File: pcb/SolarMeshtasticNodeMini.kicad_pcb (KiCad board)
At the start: 4 copper layers, 33 x 47 mm, 30 parts, among them J2 Conn_01x02_Socket, J3 Conn_01x04_Socket, J4 Conn_01x02_Pin, J5 Conn_01x04_Socket, SW1 SSSS811101, SW2 SW_Push, U1 BQ25185, U2 HT-CT62, U3 HE9073A30MR, U4 APX803L05-32SA-7, U9 SS26_C5350986

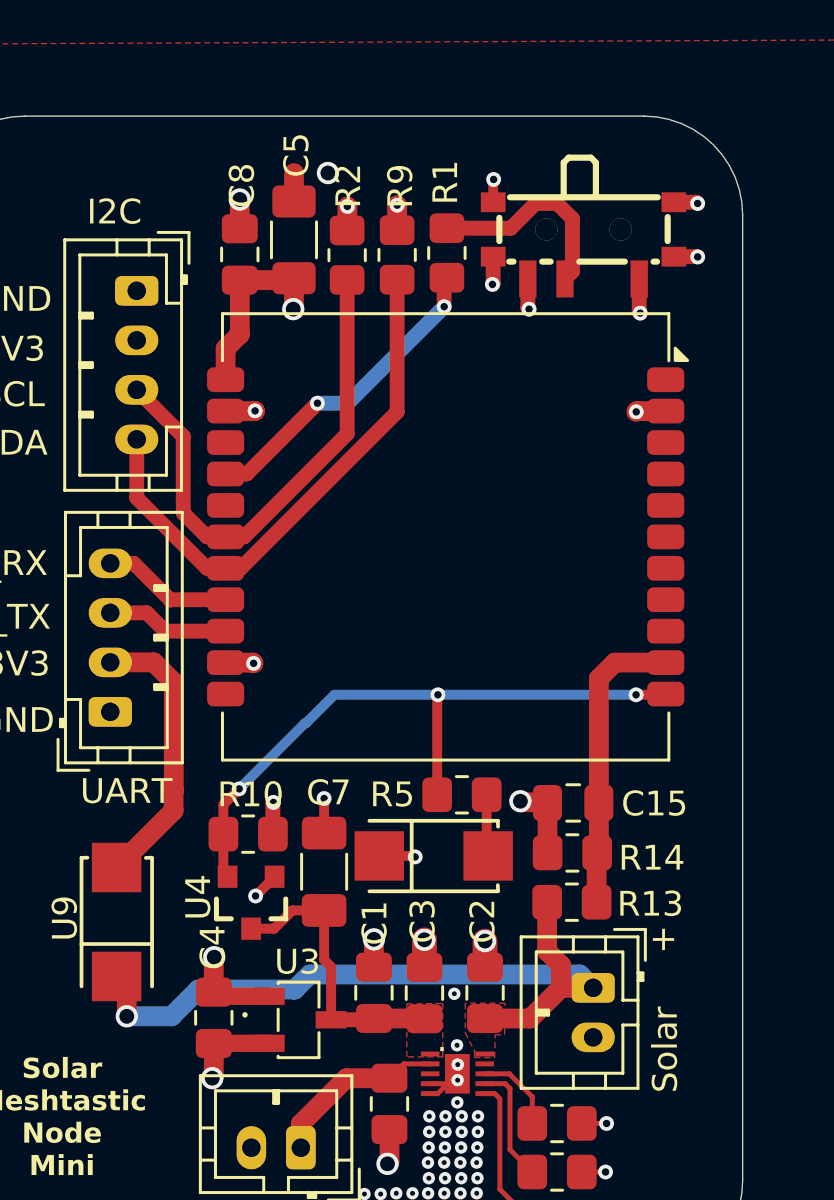
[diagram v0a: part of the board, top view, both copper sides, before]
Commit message: pcb: fix some missing .steps and move silk prints around
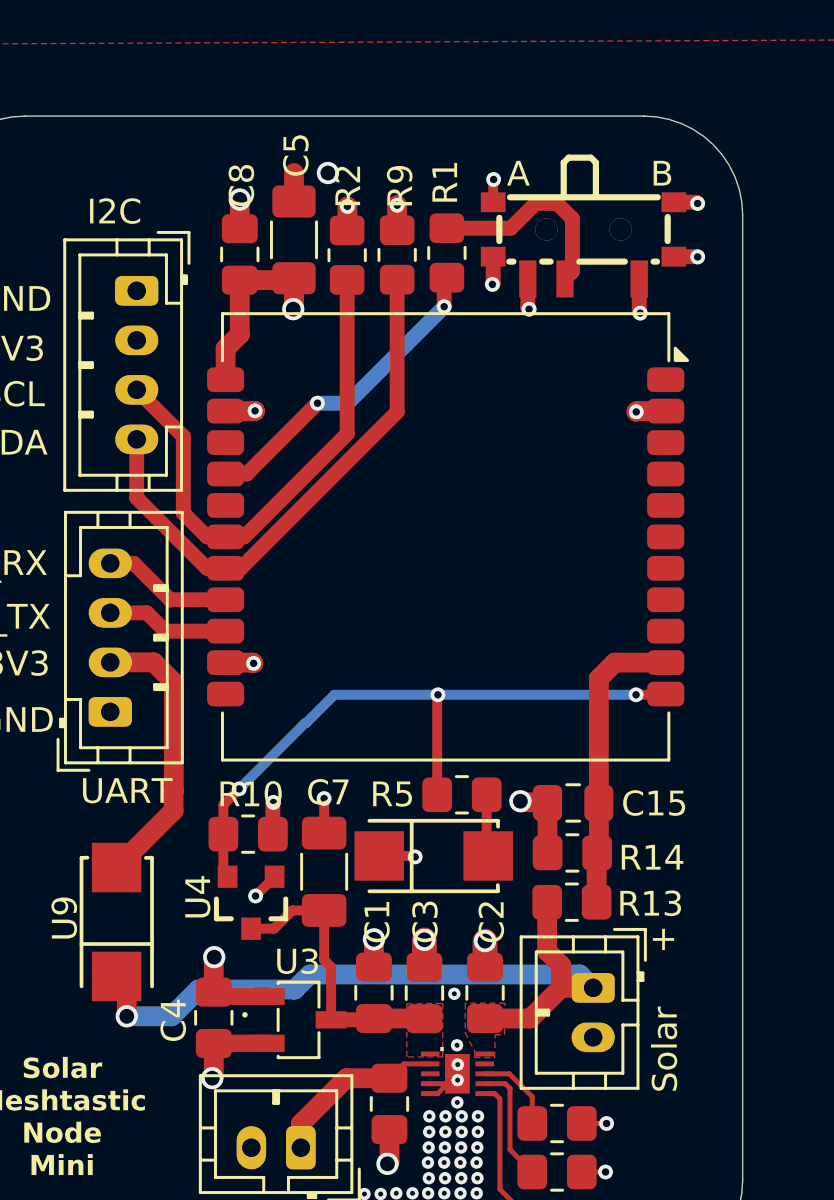
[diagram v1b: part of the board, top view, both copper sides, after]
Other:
- board text added: "A"
- board text added: "B"
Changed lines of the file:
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@@
 		(tags "capacitor handsolder")
 		(property "Reference" "C2"
-			(at -2.9025 0.09 90)
+			(at -2.8825 -0.29 90)
 			(layer "F.SilkS")
 			(effects
@@
 		(tags "capacitor handsolder")
 		(property "Reference" "C4"
-			(at 2.85 -0.03 90)
+			(at -0.1 -1.6025 90)
 			(layer "F.SilkS")
 			(effects
@@
 		)
 		(embedded_fonts no)
+		(model "${KICAD9_3DMODEL_DIR}/Package_TO_SOT_SMD.3dshapes/SOT-23-3.step"
+			(offset
+				(xyz 0 0 0)
+			)
+			(scale
+				(xyz 1 1 1)
+			)
+			(rotate
+				(xyz -0 -0 -90)
+			)
+		)
 	)
 	(footprint "Resistor_SMD:R_0805_2012Metric_Pad1.20x1.40mm_HandSolder"
@@
 		(tags "capacitor handsolder")
 		(property "Reference" "C3"
-			(at -2.91 0.06 90)
+			(at -2.89 -0.0575 90)
 			(layer "F.SilkS")
 			(effects
@@
 		(tags "capacitor handsolder")
 		(property "Reference" "C1"
-			(at 2.82 0.04 90)
+			(at 2.88 0.1575 90)
 			(layer "F.SilkS")
 			(effects
@@
 		)
 	)
+	(gr_text "A"
+		(at 234.97 32.93 0)
+		(layer "F.SilkS")
+		(effects
+			(font
+				(size 1 1)
+				(thickness 0.125)
+			)
+			(justify left bottom)
+		)
+	)
 	(gr_text "+"
 		(at 240.74903 62.69 270)
@@
 			)
 			(justify left bottom)
+		)
+	)
+	(gr_text "B"
+		(at 240.77 32.93 0)
+		(layer "F.SilkS")
+		(effects
+			(font
+				(size 1 1)
+				(thickness 0.125)
+			)
+			(justify left bottom)

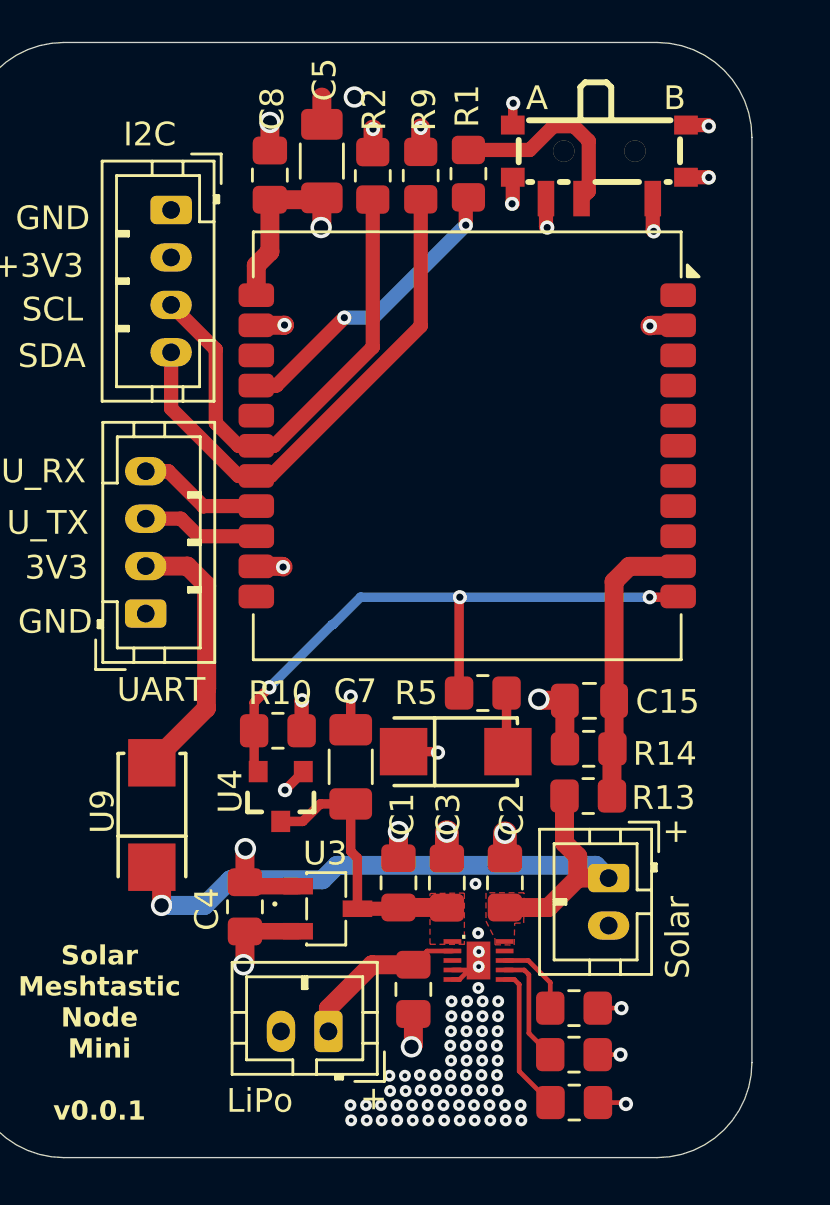
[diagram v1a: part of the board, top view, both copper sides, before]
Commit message: pcb, sch: use VLOAD and not VBUS for ADC
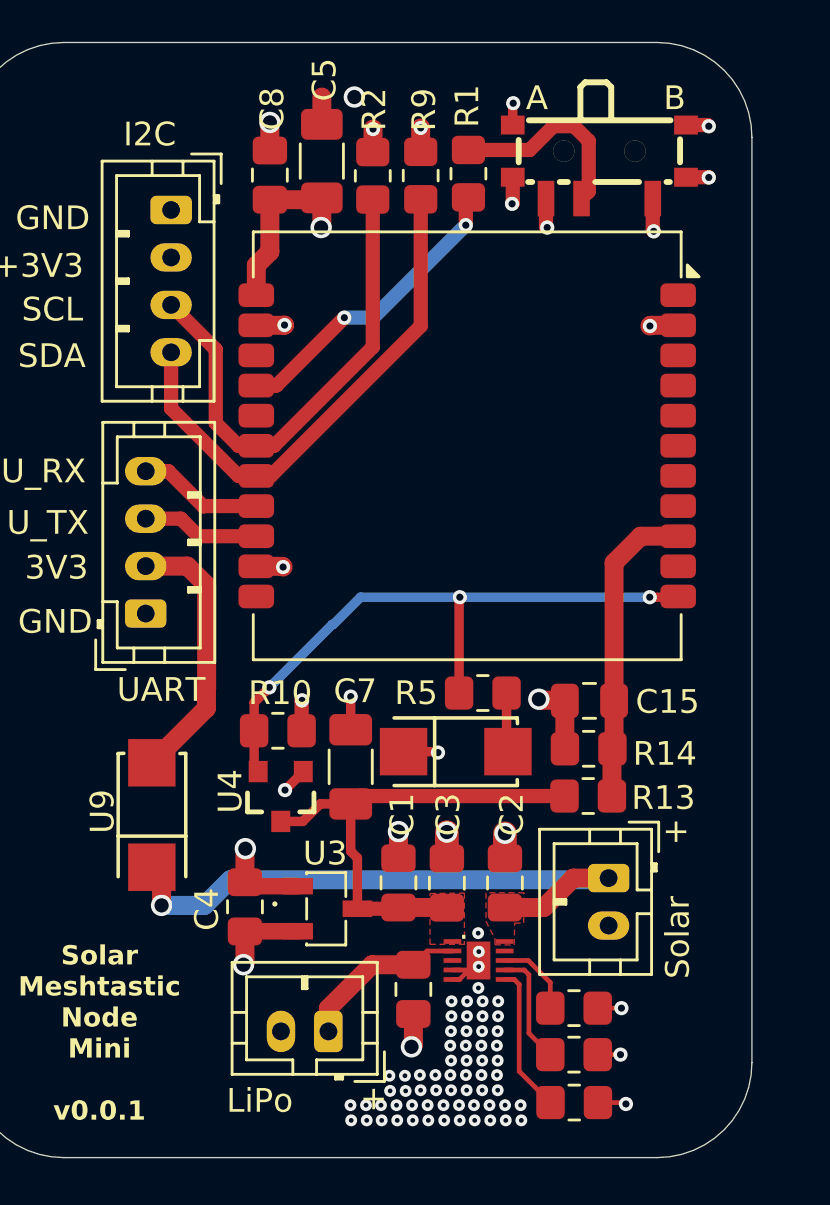
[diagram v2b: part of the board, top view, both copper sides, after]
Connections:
- C15 pad 1: /ADC_VBUS -> /ADC_LOAD
- R13 pad 1: /VBUS -> /VLOAD
- R13 pad 2: /ADC_VBUS -> /ADC_LOAD
- R14 pad 1: /ADC_VBUS -> /ADC_LOAD
- U2 pad 10: /ADC_VBUS -> unconnected-(U2-GPIO0-Pad10)
- U2 pad 9: unconnected-(U2-GPIO1-Pad9) -> /ADC_LOAD
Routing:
- net /ADC_LOAD: track 0.00 -> 13.0 mm
- net /ADC_VBUS: track 12.0 -> 0.00 mm
- net /VLOAD: track 11.6 -> 20.2 mm
- net /VBUS: track 30.4 -> 25.4 mm
- net GND: track 32.5 -> 31.8 mm, vias 87 -> 86

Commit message: pcb, jpg: small eyecandy works
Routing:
- net GND: vias 86 -> 129

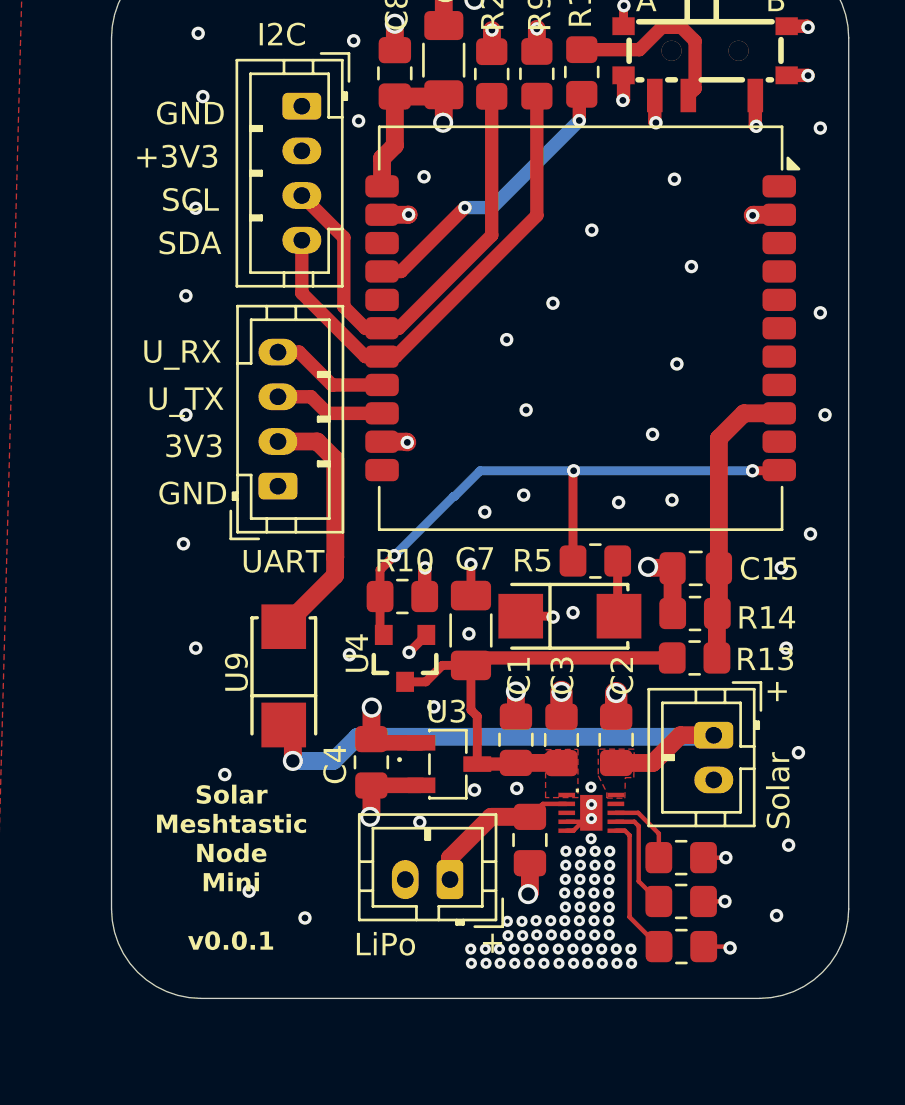
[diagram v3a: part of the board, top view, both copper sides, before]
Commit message: pcb: add missing silk prints
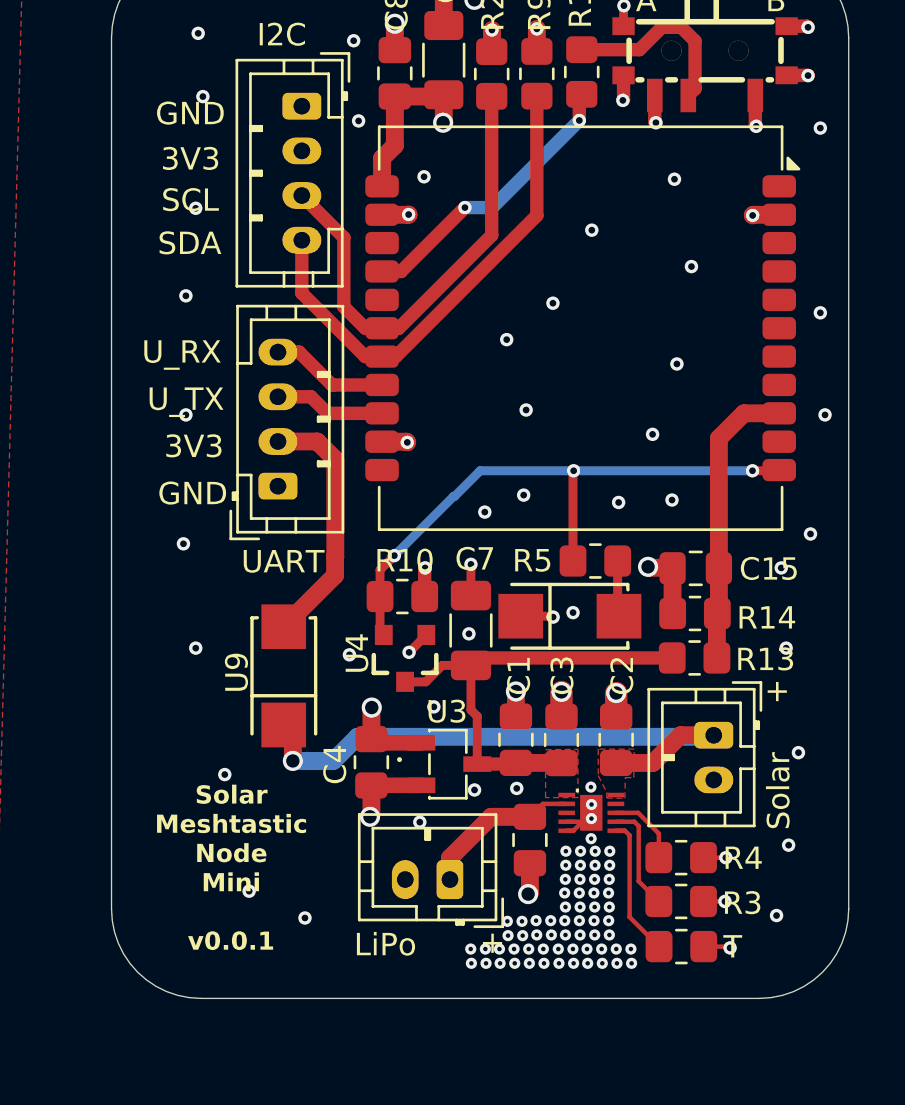
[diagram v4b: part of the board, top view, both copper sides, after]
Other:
- board text added: "T"
- board text removed: "+3V3"
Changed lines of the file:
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@@
 		(tags "resistor handsolder")
 		(property "Reference" "R6"
-			(at 0 -1.65 0)
+			(at 2.79 0 0)
 			(layer "F.SilkS")
 			(hide yes)
@@
 		(tags "resistor handsolder")
 		(property "Reference" "R4"
-			(at 0.08375 -1.67 0)
+			(at 2.77 0.04 0)
 			(layer "F.SilkS")
-			(hide yes)
 			(effects
 				(font
@@
 		(tags "resistor handsolder")
 		(property "Reference" "R3"
-			(at -0.02625 1.78 0)
+			(at 2.74 0.09 0)
 			(layer "F.SilkS")
-			(hide yes)
 			(effects
 				(font
@@
 		)
 	)
-	(gr_text "+3V3"
-		(at 212.507619 39.926667 0)
+	(gr_text "3V3"
+		(at 213.7 40.02 0)
 		(layer "F.SilkS")
 		(effects
@@
 			)
 			(justify left bottom)
+		)
+	)
+	(gr_text "T"
+		(at 238.89 75.29 0)
+		(layer "F.SilkS")
+		(effects
+			(font
+				(size 1 1)
+				(thickness 0.15)
+			)
+			(justify left bottom)

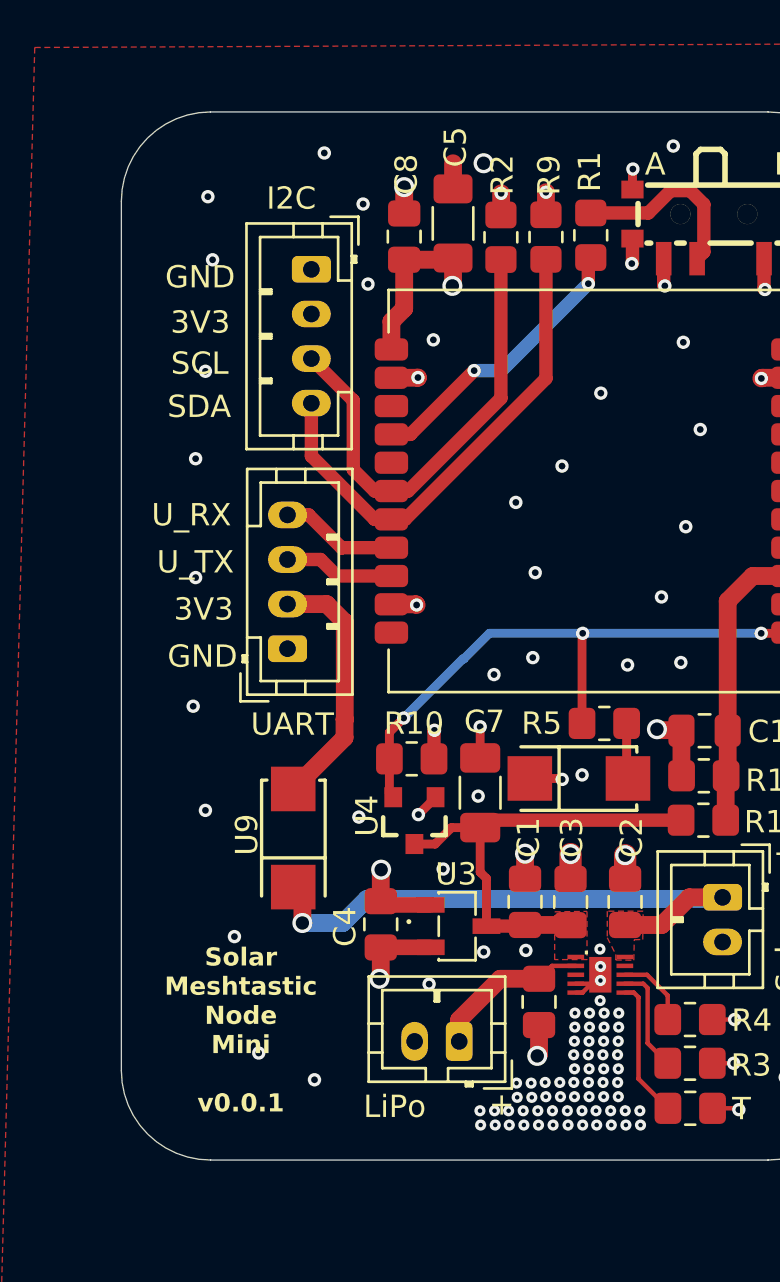
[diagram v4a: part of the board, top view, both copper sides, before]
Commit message: pcb, sch: add mounting hole (M2.5)
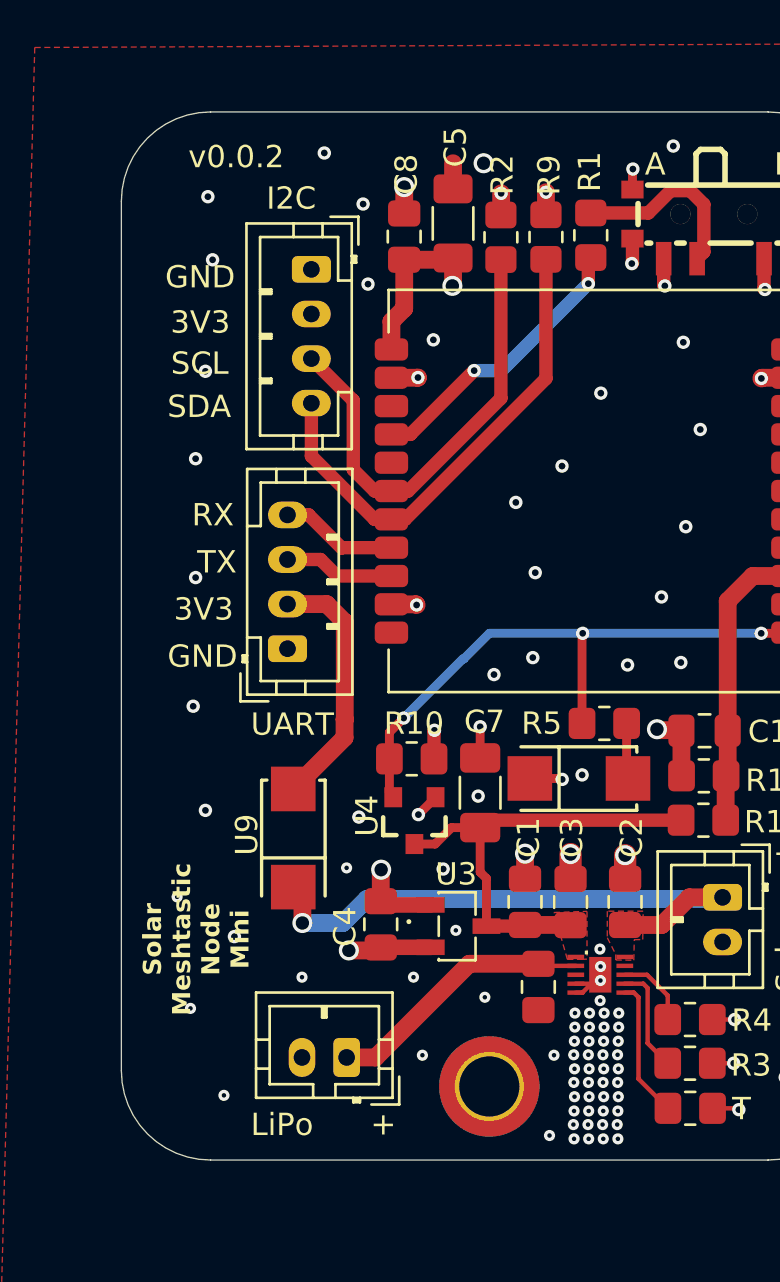
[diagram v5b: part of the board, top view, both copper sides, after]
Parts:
- added H1: MountingHole, MountingHole:MountingHole_2.7mm_M2.5_ISO14580_Pad_TopBottom, F.Cu at (228.0, 73.7)
- moved J4 5.10 mm to (221.6, 72.4)
- moved C6 0.67 mm to (230.2, 69.2)
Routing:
- net /VLIPO: track 7.20 -> 12.1 mm
- net GND: track 31.8 -> 30.4 mm, vias 129 -> 114
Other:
- board text added: "RX"
- board text added: "Solar Meshtastic Node Mini"
- board text added: "TX"
- board text added: "v0.0.2"
- board text removed: "Solar Meshtastic Node Mini v0.0.1"
- board text removed: "U_RX"
- board text removed: "U_TX"
